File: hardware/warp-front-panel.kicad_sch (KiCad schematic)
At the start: 40 parts, among them J101 Boot, P101 Debug, P102 CON-SENSOR2, Q101 2N7002P, U101 XMC1404, U102 BY25Q128ESSIG(R), U104 ESP-PSRAM64?, X101 16MHz

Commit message: drc
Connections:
- net GND: now also SW101.2; no longer SW101.4
- net SW: now also SW101.4; no longer SW101.2
- net at SW101.L1: now also R111.2; no longer R113.2
- net at SW101.L2: now also R113.2; no longer R111.2
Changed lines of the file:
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@@
 	(title_block
 		(title "WARP Front Panel")
-		(date "2024-06-21")
-		(rev "1.0")
+		(date "2024-07-02")
+		(rev "1.1")
 		(company "Tinkerforge GmbH")
 		(comment 1 "Licensed under CERN OHL v.1.1")
@@
 		(lib_id "tinkerforge:LED_TACT_SW_THT")
 		(at 108.585 111.76 0)
+		(mirror y)
 		(unit 1)
 		(exclude_from_sim no)
@@
 		(on_board yes)
 		(dnp no)
-		(fields_autoplaced yes)
 		(property "Reference" "SW101"
 			(at 108.585 104.1485 0)

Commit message: updated design V1.2
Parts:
- removed C110: 100nF, C0603F, symbol tinkerforge:C
- removed R105, R106: 82, kicad-libraries:R0603F, symbol tinkerforge:R
- removed SW101: ~, kicad-libraries:LED_TACT_SW_THT, symbol tinkerforge:LED_TACT_SW_THT
- removed U104: ESP-PSRAM64?, kicad-libraries:SO-8, symbol tinkerforge:S25FLXXX
- added Pw1, Pw2: CONN_01X04, tf:pin_array_1x4-P2mm_D1mm, symbol tf:CONN_01X04
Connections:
- net GND: now also Pw1.1 (P1), Pw1.4 (P4), Pw2.1 (P1), Pw2.3 (P3), Pw2.4 (P4)
- net SW: now also Pw2.2 (P2)
- net SW-LED2: now reaches R111.2
- net SW-LED2: now also Pw1.3 (P3)
- net SW-LED1: now reaches R113.2
- net SW-LED1: now also Pw1.2 (P2)
- no-connect marks 25 -> 23
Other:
- note removed: "23AA04M"
- note removed: "TODO RGB LED + Tact Switch"
- moved on the sheet: R111, R112, R113

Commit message: improve routing
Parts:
- removed R113: 220, kicad-libraries:R0603F, symbol tinkerforge:R
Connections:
- net SW-LED1: now also U101.21 (P1.5_IHO)
- net at U101.15 (P2.12/AIO): no longer R108.1
- net at U101.4 (P2.1_AIO): now also R108.1
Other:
- moved on the sheet: R108
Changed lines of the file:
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@@
 	)
 	(no_connect
-		(at 129.54 123.19)
-	)
-	(no_connect
 		(at 217.17 137.16)
 	)
@@
 	)
 	(no_connect
+		(at 129.54 151.13)
+	)
+	(no_connect
 		(at 129.54 148.59)
 	)
@@
 	(wire
 		(pts
+			(xy 114.3 105.41) (xy 129.54 105.41)
+		)
+		(stroke
+			(width 0)
+			(type default)
+		)
+	)
+	(wire
+		(pts
 			(xy 92.71 20.32) (xy 92.71 21.59)
 		)
@@
 	(wire
 		(pts
-			(xy 111.76 151.13) (xy 114.3 151.13)
+			(xy 111.76 123.19) (xy 114.3 123.19)
 		)
 		(stroke
@@
 	(wire
 		(pts
-			(xy 127 151.13) (xy 129.54 151.13)
+			(xy 127 123.19) (xy 129.54 123.19)
 		)
 		(stroke
@@
 	(wire
 		(pts
-			(xy 127 105.41) (xy 129.54 105.41)
-		)
-		(stroke
-			(width 0)
-			(type default)
-		)
-	)
-	(wire
-		(pts
 			(xy 215.9 119.38) (xy 217.17 119.38)
 		)
@@
 	(global_label "nWP"
 		(shape output)
-		(at 111.76 151.13 180)
+		(at 111.76 123.19 180)
 		(fields_autoplaced yes)
 		(effects
@@
 		)
 		(property "Intersheetrefs" "${INTERSHEET_REFS}"
-			(at 106.4128 151.13 0)
+			(at 106.4128 123.19 0)
 			(effects
 				(font
@@
 	)
 	(symbol
-		(lib_id "tinkerforge:R")
-		(at 120.65 105.41 270)
-		(mirror x)
-		(unit 1)
-		(exclude_from_sim no)
-		(in_bom yes)
-		(on_board yes)
-		(dnp no)
-		(property "Reference" "R113"
-			(at 118.11 102.87 90)
-			(effects
-				(font
-					(size 1.27 1.27)
-				)
-			)
-		)
-		(property "Value" "220"
-			(at 120.65 105.41 90)
-			(effects
-				(font
-					(size 1.27 1.27)
-				)
-			)
-		)
-		(property "Footprint" "kicad-libraries:R0603F"
-			(at 120.65 105.41 0)
-			(effects
-				(font
-					(size 1.524 1.524)
-				)
-				(hide yes)
-			)
-		)
-		(property "Datasheet" ""
-			(at 120.65 105.41 0)
-			(effects
-				(font
-					(size 1.524 1.524)
-				)
-			)
-		)
-		(property "Description" ""
-			(at 120.65 105.41 0)
-			(effects
-				(font
-					(size 1.27 1.27)
-				)
-				(hide yes)
-			)
-		)
-		(pin "1"
-		)
-		(pin "2"
-		)
-		(instances
-			(project "warp-front-panel"
-				(path "/6f95f6fd-d127-4f29-b004-e8df75ff7108"
-					(reference "R113")
-					(unit 1)
-				)
-			)
-		)
-	)
-	(symbol
 		(lib_id "tinkerforge:ER-TFT020")
 		(at 217.17 120.65 0)
@@
 	(symbol
 		(lib_id "tinkerforge:R")
-		(at 120.65 151.13 270)
+		(at 120.65 123.19 270)
 		(mirror x)
 		(unit 1)
@@
 		(dnp no)
 		(property "Reference" "R108"
-			(at 120.65 148.59 90)
+			(at 120.65 125.73 90)
 			(effects
 				(font
@@
 		)
 		(property "Value" "82"
-			(at 120.65 151.13 90)
+			(at 120.65 123.19 90)
 			(effects
 				(font
@@
 		)
 		(property "Footprint" "kicad-libraries:R0603F"
-			(at 120.65 151.13 0)
+			(at 120.65 123.19 0)
 			(effects
 				(font
@@
 		)
 		(property "Datasheet" ""
-			(at 120.65 151.13 0)
+			(at 120.65 123.19 0)
 			(effects
 				(font
@@
 		)
 		(property "Description" ""
-			(at 120.65 151.13 0)
+			(at 120.65 123.19 0)
 			(effects
 				(font

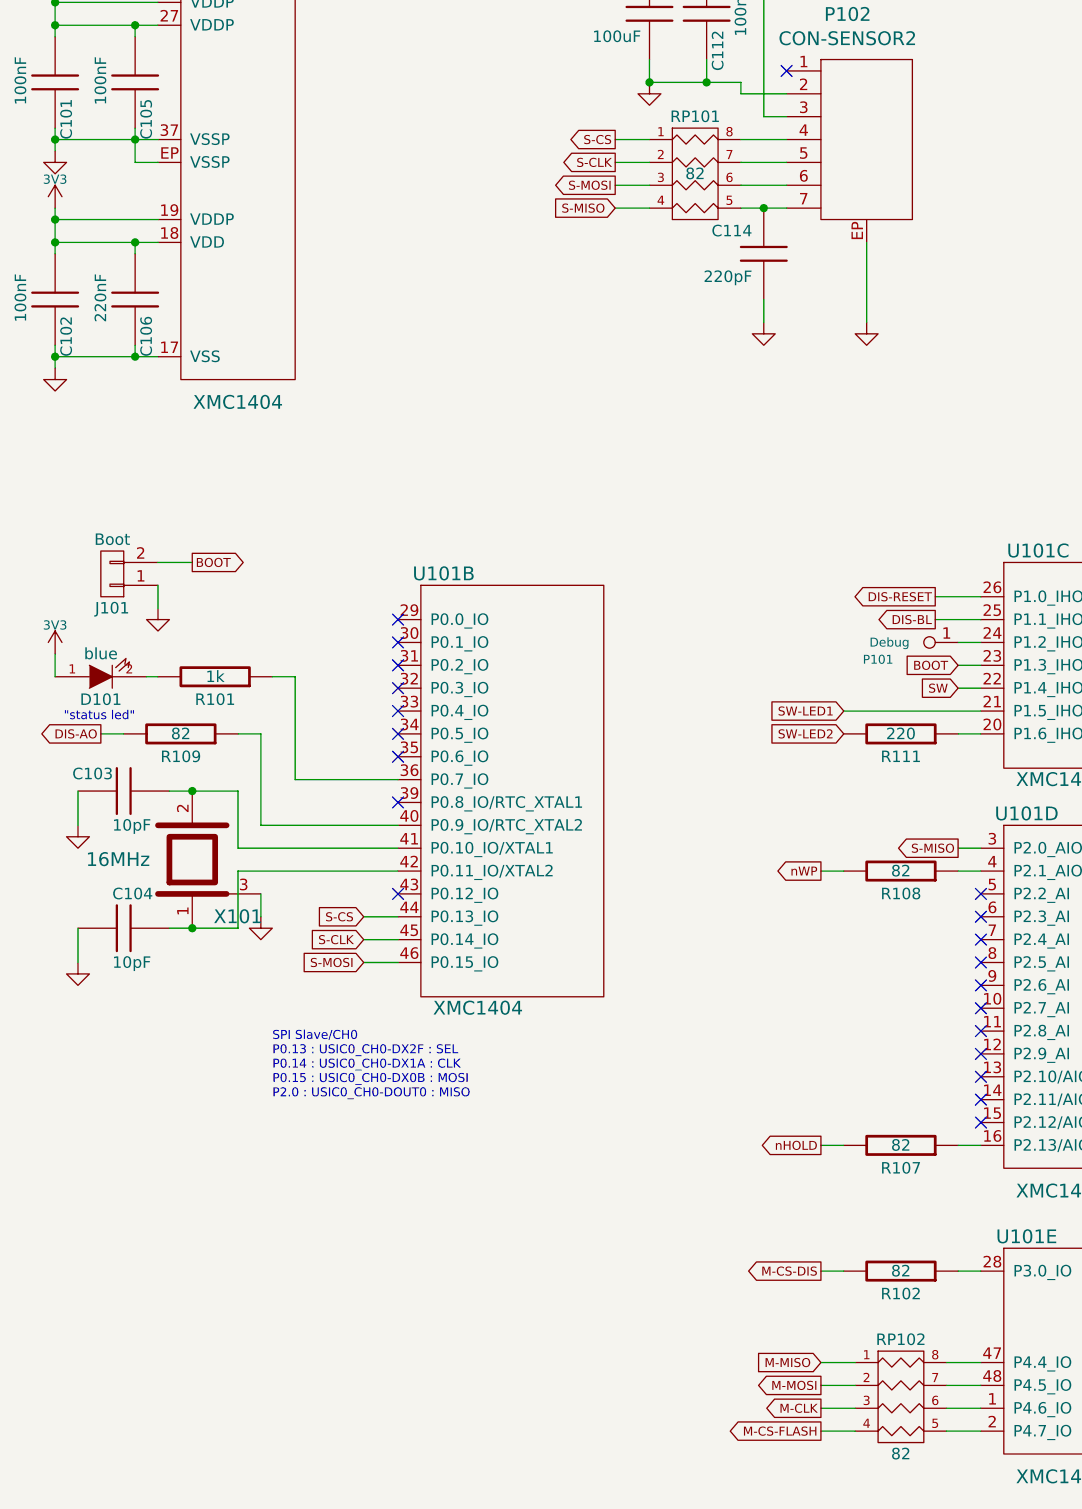
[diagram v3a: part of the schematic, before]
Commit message: changed data resistor values to 4,7Ohm
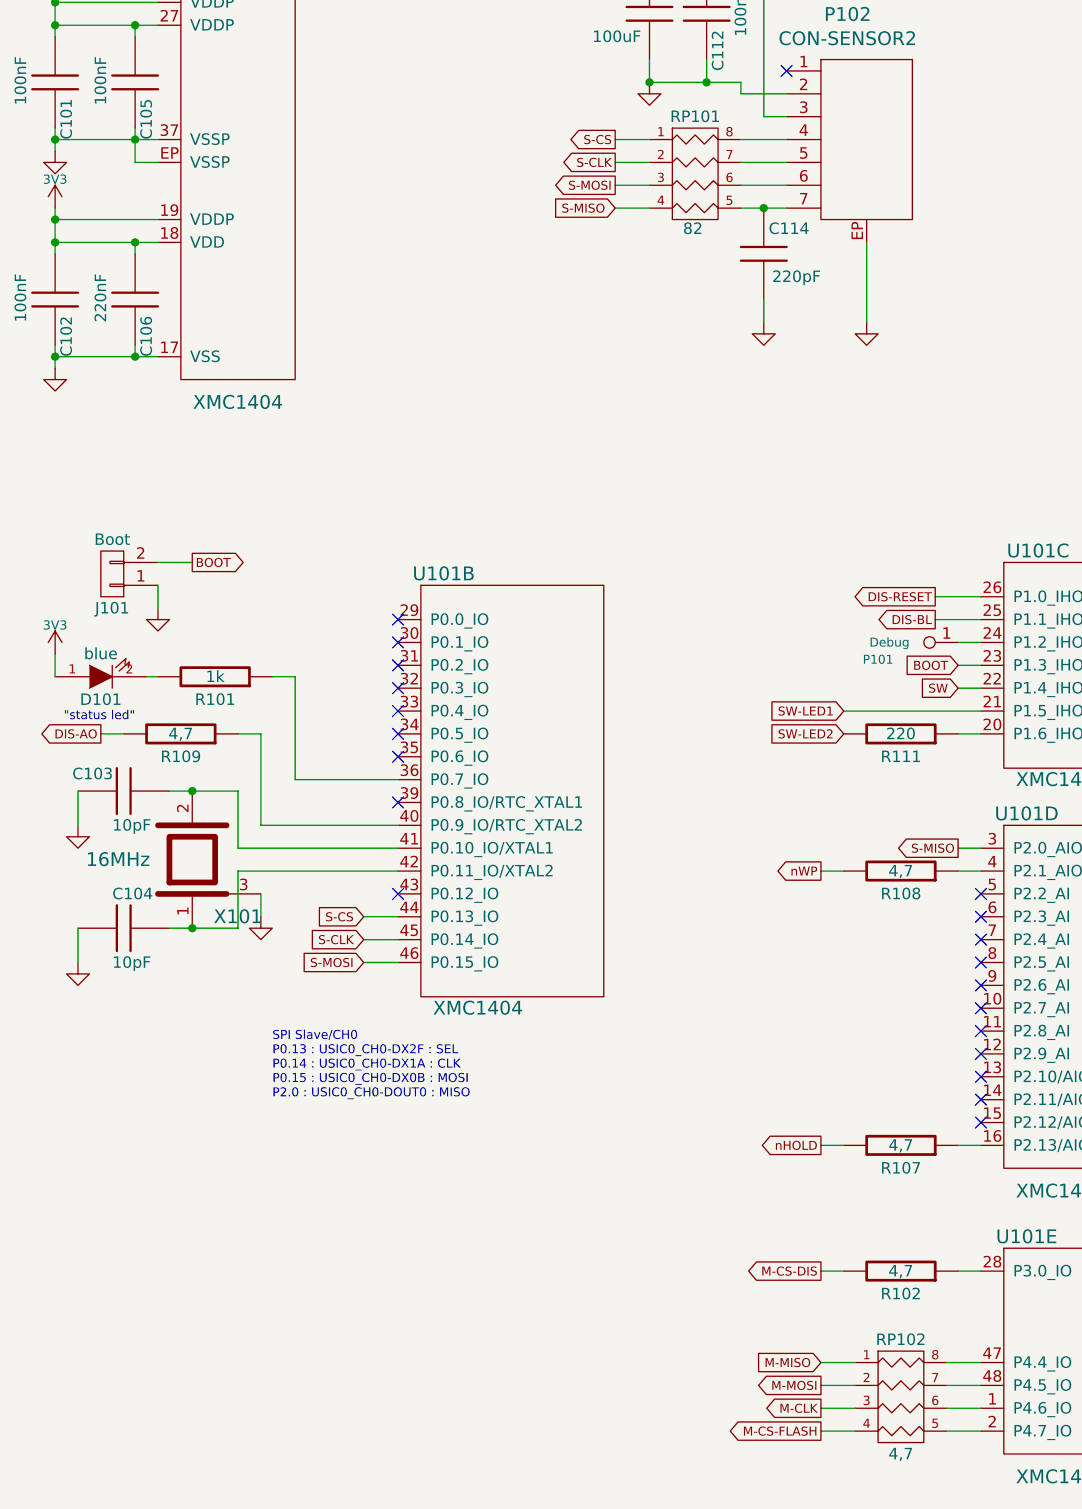
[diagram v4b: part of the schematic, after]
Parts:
- R102, R107, R108, R109, RP102: value 82 -> 4,7
- U103: TFX (none) -> TFX-06-204
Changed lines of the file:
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@@
 		(dnp no)
 		(property "Reference" "C114"
-			(at 104.14 52.07 0)
+			(at 110.49 51.816 0)
 			(effects
 				(font
@@
 		)
 		(property "Value" "220pF"
-			(at 104.14 57.15 0)
+			(at 111.76 57.15 0)
 			(effects
 				(font
@@
 			)
 		)
-		(property "Value" "82"
+		(property "Value" "4,7"
 			(at 120.65 167.64 90)
 			(effects
@@
 		)
 		(property "Description" ""
+			(at 120.65 167.64 0)
+			(effects
+				(font
+					(size 1.27 1.27)
+				)
+				(hide yes)
+			)
+		)
+		(property "TFX" ""
 			(at 120.65 167.64 0)
 			(effects
@@
 			)
 		)
+		(property "TFX" "TFX-06-204"
+			(at 217.17 120.65 0)
+			(effects
+				(font
+					(size 1.27 1.27)
+				)
+				(hide yes)
+			)
+		)
 		(pin "10"
 		)
@@
 		)
 		(property "Value" "82"
-			(at 97.79 45.72 0)
+			(at 97.536 51.816 0)
 			(effects
 				(font
@@
 			)
 		)
-		(property "Value" "82"
+		(property "Value" "4,7"
 			(at 40.64 107.95 90)
 			(effects
@@
 		)
 		(property "Description" ""
+			(at 40.64 107.95 0)
+			(effects
+				(font
+					(size 1.27 1.27)
+				)
+				(hide yes)
+			)
+		)
+		(property "TFX" ""
 			(at 40.64 107.95 0)
 			(effects
@@
 			)
 		)
-		(property "Value" "82"
+		(property "Value" "4,7"
 			(at 120.65 123.19 90)
 			(effects
@@
 			)
 		)
-		(property "Value" "82"
+		(property "Value" "4,7"
 			(at 120.65 153.67 90)
 			(effects
@@
 			)
 		)
-		(property "Value" "82"
+		(property "Value" "4,7"
 			(at 120.65 187.96 0)
 			(effects
